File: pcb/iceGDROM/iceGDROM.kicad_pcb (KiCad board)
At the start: 2 copper layers, 60 x 40 mm, 76 parts, among them J1 Conn_02x22_Odd_Even, J2 Micro_SD_Card_Det_Hirose_DM3AT, U1 ICE40HX8K-BG121, U2 ME6206A25M3G_SOT23, U3 LD1117S12TR_SOT223, U4 W25Q32JVSS, X1 SG-310SCF

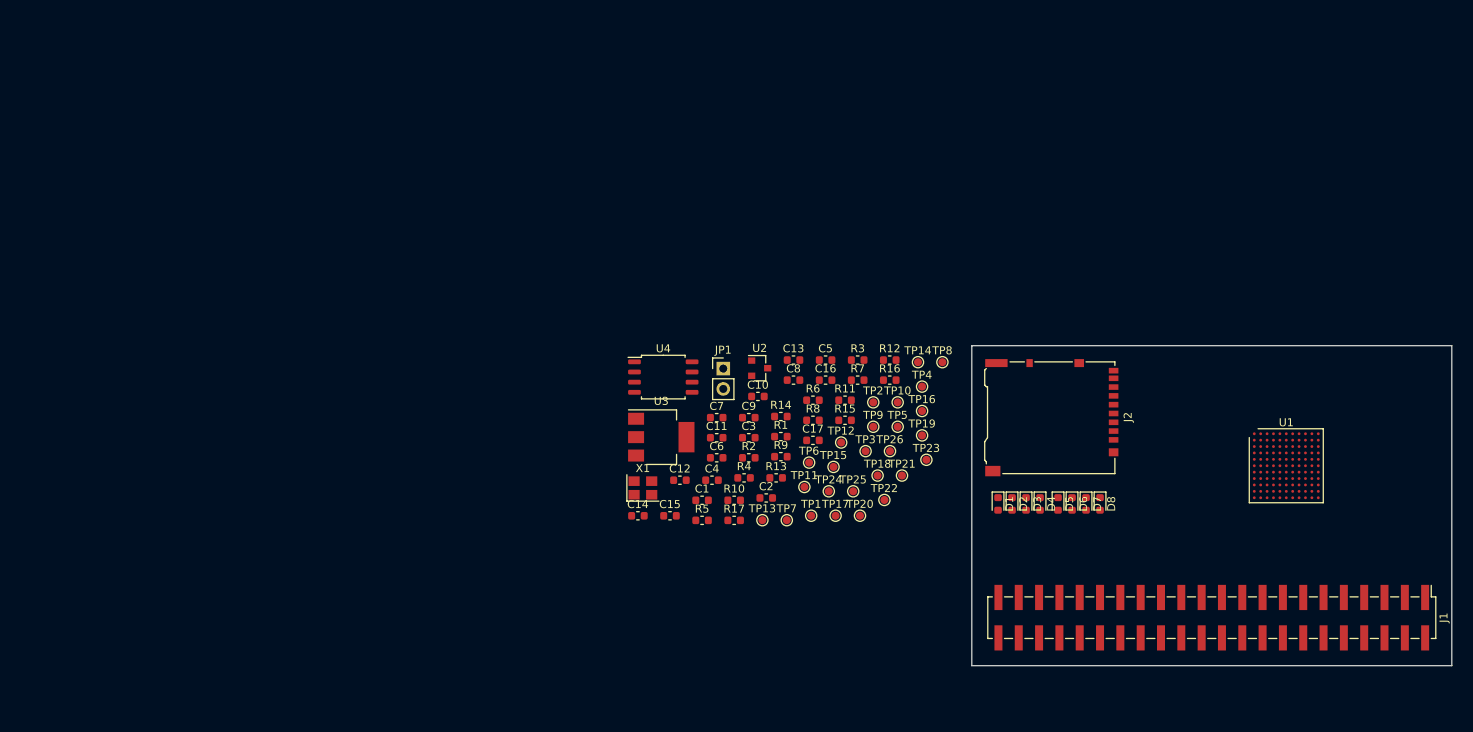
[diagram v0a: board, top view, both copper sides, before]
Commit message: Included the SPI Memory card into the schematic as a major point. Created a footprint for the tactile button being used and including the 3D model due to no NC clause.
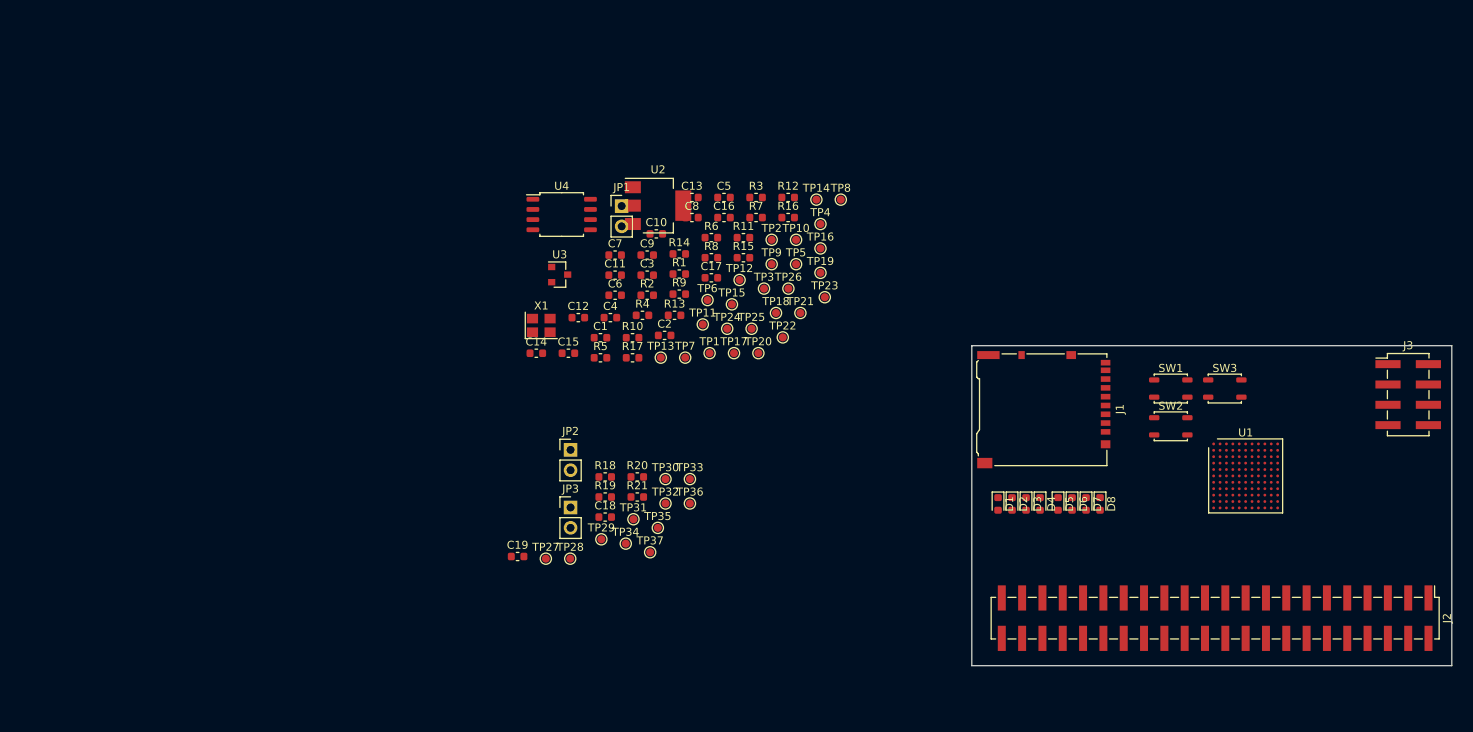
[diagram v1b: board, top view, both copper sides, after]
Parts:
- added C18: 1u0, Capacitor_SMD:C_0603_1608Metric, F.Cu at (109.2, 86.4)
- added C19: 10u, Capacitor_SMD:C_0603_1608Metric, F.Cu at (98.2, 91.4)
- added J3: Conn_02x04_Odd_Even, Connector_PinHeader_2.54mm:PinHeader_2x04_P2.54mm_Vertical_SMD, F.Cu at (209.6, 71.1)
- added JP2: Jumper_NC_Small, Connector_PinHeader_2.54mm:PinHeader_1x02_P2.54mm_Vertical, F.Cu at (104.8, 78.0)
- added JP3: Jumper_NC_Small, Connector_PinHeader_2.54mm:PinHeader_1x02_P2.54mm_Vertical, F.Cu at (104.8, 85.2)
- added R18: 10K, Resistor_SMD:R_0603_1608Metric, F.Cu at (109.2, 81.4)
- added R19: 10K, Resistor_SMD:R_0603_1608Metric, F.Cu at (109.2, 83.9)
- added R20: 100R, Resistor_SMD:R_0603_1608Metric, F.Cu at (113.2, 81.4)
- added R21: 100R, Resistor_SMD:R_0603_1608Metric, F.Cu at (113.2, 83.9)
- added SW1: SW_Push, iceGDROM:SW_Push_SPST_NO_Alps_SKRP, F.Cu at (179.9, 70.4)
- added SW2: SW_Push, iceGDROM:SW_Push_SPST_NO_Alps_SKRP, F.Cu at (179.9, 75.1)
- added SW3: SW_Push, iceGDROM:SW_Push_SPST_NO_Alps_SKRP, F.Cu at (186.6, 70.4)
- added TP27: TestPoint, TestPoint:TestPoint_Pad_D1.0mm, F.Cu at (101.8, 91.6)
- added TP28: TestPoint, TestPoint:TestPoint_Pad_D1.0mm, F.Cu at (104.8, 91.6)
- added TP29: TestPoint, TestPoint:TestPoint_Pad_D1.0mm, F.Cu at (108.7, 89.2)
- added TP30: TestPoint, TestPoint:TestPoint_Pad_D1.0mm, F.Cu at (116.7, 81.7)
- added TP31: TestPoint, TestPoint:TestPoint_Pad_D1.0mm, F.Cu at (112.7, 86.7)
- added TP32: TestPoint, TestPoint:TestPoint_Pad_D1.0mm, F.Cu at (116.7, 84.7)
- added TP33: TestPoint, TestPoint:TestPoint_Pad_D1.0mm, F.Cu at (119.8, 81.7)
- added TP34: TestPoint, TestPoint:TestPoint_Pad_D1.0mm, F.Cu at (111.7, 89.7)
- added TP35: TestPoint, TestPoint:TestPoint_Pad_D1.0mm, F.Cu at (115.8, 87.8)
- added TP36: TestPoint, TestPoint:TestPoint_Pad_D1.0mm, F.Cu at (119.8, 84.7)
- added TP37: TestPoint, TestPoint:TestPoint_Pad_D1.0mm, F.Cu at (114.8, 90.8)
- C11, C12, C17, C2: value 10u -> 100n
- C15, C16, C5: value 100n -> 10u
- C3: value 1u0 -> 10u
- C4: value 100n -> 1u0
- C6: value 10u -> 1u0
- C7: value 1u0 -> 100n
- J1: value Conn_02x22_Odd_Even -> Micro_SD_Card_Det_Hirose_DM3AT; footprint Connector_PinHeader_2.54mm:PinHeader_2x22_P2.54mm_Vertical_SMD -> Connector_Card:microSD_HC_Hirose_DM3AT-SF-PEJM5
- J2: value Micro_SD_Card_Det_Hirose_DM3AT -> Conn_02x22_Odd_Even; footprint Connector_Card:microSD_HC_Hirose_DM3AT-SF-PEJM5 -> Connector_PinHeader_2.54mm:PinHeader_2x22_P2.54mm_Vertical_SMD
- R1, R12, R13, R14, R15, R16, R17, R2, R3, R4, R5, R6, R7, R8: value R -> 10K
- R10, R9: value 100R -> 10K
- U2: value ME6206A25M3G_SOT23 -> LD1117S12TR_SOT223; footprint Package_TO_SOT_SMD:SOT-23 -> Package_TO_SOT_SMD:SOT-223-3_TabPin2
- U3: value LD1117S12TR_SOT223 -> ME6206A25M3G_SOT23; footprint Package_TO_SOT_SMD:SOT-223-3_TabPin2 -> Package_TO_SOT_SMD:SOT-23
- moved J1 33.4 mm to (164.0, 73.0)
- moved J2 32.3 mm to (185.4, 99.1)
- moved R7 24.0 mm to (128.0, 49.0)
- moved TP10 24.0 mm to (133.0, 51.8)
- moved C17 24.0 mm to (122.4, 56.5)
- moved C8 24.0 mm to (120.0, 49.0)
- moved JP1 24.0 mm to (111.2, 47.5)
- moved R10 24.0 mm to (112.6, 64.0)
- moved R13 24.0 mm to (117.8, 61.2)
- moved R17 24.0 mm to (112.6, 66.5)
- moved R3 24.0 mm to (128.0, 46.5)
- moved TP21 24.0 mm to (133.6, 60.9)
- moved TP26 24.0 mm to (132.1, 57.9)
- moved TP5 24.0 mm to (133.0, 54.8)
- moved C10 24.0 mm to (115.6, 51.0)
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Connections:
- net Net-(R4-Pad2) renamed /LED0
- net Net-(R5-Pad2) renamed /LED1
- net Net-(R6-Pad2) renamed /LED2
- net Net-(R7-Pad2) renamed /LED3
- C10 pad 1: Net-(C10-Pad1) -> +1V2
- C10 pad 2: Net-(C10-Pad2) -> GND
- C11 pad 1: Net-(C11-Pad1) -> +1V2
- C11 pad 2: Net-(C11-Pad2) -> GND
- C12 pad 1: Net-(C10-Pad1) -> Net-(C12-Pad1)
- C12 pad 2: Net-(C10-Pad2) -> Net-(C12-Pad2)
- C13 pad 1: +1V2 -> Net-(C13-Pad1)
- C13 pad 2: GND -> Net-(C13-Pad2)
- C15 pad 1: +1V2 -> Net-(C12-Pad1)
- C15 pad 2: GND -> Net-(C12-Pad2)
- C16 pad 1: +1V2 -> Net-(C13-Pad1)
- C16 pad 2: GND -> Net-(C13-Pad2)
- C5 pad 1: +3V3 -> +1V2
- C6 pad 1: +1V2 -> +2V5
- C7 pad 1: +2V5 -> +3V3
- C8 pad 1: +2V5 -> +3V3
- C9 pad 1: Net-(C11-Pad1) -> +2V5
- C9 pad 2: Net-(C11-Pad2) -> GND
- J1 pad 1: /G_RST -> /PB5
- J1 pad 10: /D11 -> /PB7
- J1 pad 11: /D3 -> GND
- J1 pad 2: GND -> /PB6
- J1 pad 3: /D7 -> /PB2
- J1 pad 4: /D8 -> +3V3
- J1 pad 5: /D6 -> /PB1
- J1 pad 6: /D9 -> GND
- J1 pad 7: /D5 -> /PB3
- J1 pad 8: /D10 -> /PB4
- J1 pad 9: /D4 -> GND
- J2 pad 1: Net-(J2-Pad1) -> /G_RST
- J2 pad 10: Net-(J2-Pad10) -> /D11
- J2 pad 11: Net-(J2-Pad11) -> /D3
- J2 pad 2: Net-(J2-Pad2) -> GND
- J2 pad 3: Net-(J2-Pad3) -> /D7
- J2 pad 4: Net-(J2-Pad4) -> /D8
- J2 pad 5: Net-(J2-Pad5) -> /D6
- J2 pad 6: Net-(J2-Pad6) -> /D9
- J2 pad 7: Net-(J2-Pad7) -> /D5
- J2 pad 8: Net-(J2-Pad8) -> /D10
- J2 pad 9: Net-(J2-Pad9) -> /D4
- JP1 pad 2: Net-(JP1-Pad2) -> /FLASH_CSn
- R1 pad 1: Net-(D1-Pad2) -> +3V3
- R1 pad 2: Net-(R1-Pad2) -> /PB7
- R10 pad 1: +1V2 -> Net-(D6-Pad2)
- R10 pad 2: Net-(C10-Pad1) -> /LED5
- R11 pad 1: Net-(R11-Pad1) -> Net-(D7-Pad2)
- R11 pad 2: +3V3 -> /LED6
- R12 pad 1: +3V3 -> Net-(D8-Pad2)
- R12 pad 2: /FPGA_SCK -> /LED7
- R13 pad 1: +3V3 -> Net-(R13-Pad1)
- R13 pad 2: Net-(JP1-Pad2) -> +3V3
- R14 pad 2: Net-(R14-Pad2) -> /FPGA_SCK
- R15 pad 2: Net-(R15-Pad2) -> /FLASH_CSn
- R16 pad 2: Net-(R16-Pad2) -> /FLASH_MOSI|IO0
- R17 pad 2: Net-(R17-Pad2) -> /FLASH_MISO|IO1
- R2 pad 1: Net-(D2-Pad2) -> Net-(R2-Pad1)
- R2 pad 2: Net-(R2-Pad2) -> +3V3
- R3 pad 1: Net-(D3-Pad2) -> GND
- R4 pad 1: Net-(D4-Pad2) -> Net-(D1-Pad2)
- R5 pad 1: Net-(D5-Pad2) -> Net-(D2-Pad2)
- R6 pad 1: Net-(D6-Pad2) -> Net-(D3-Pad2)
- R7 pad 1: Net-(D7-Pad2) -> Net-(D4-Pad2)
- R8 pad 1: Net-(D8-Pad2) -> GND
- R9 pad 1: +1V2 -> Net-(D5-Pad2)
- R9 pad 2: Net-(C11-Pad1) -> /LED4
- TP17 pad 1: Net-(JP1-Pad2) -> /PB0
- TP18 pad 1: /FPGA_SCK -> /PB1
- TP19 pad 1: +1V2 -> /PB2
- TP20 pad 1: +2V5 -> /PB3
- TP21 pad 1: Net-(R14-Pad2) -> /PB4
- TP22 pad 1: Net-(C11-Pad1) -> /PB5
- TP23 pad 1: Net-(C10-Pad1) -> /PB6
- TP24 pad 1: Net-(R15-Pad2) -> /PB7
- TP25 pad 1: Net-(R16-Pad2) -> +12V
- TP26 pad 1: Net-(R17-Pad2) -> +5V
- U1 pad C5: Net-(C10-Pad2) -> Net-(C13-Pad2)
- U1 pad C6: Net-(C10-Pad1) -> Net-(C13-Pad1)
- U1 pad J6: Net-(C11-Pad1) -> Net-(C12-Pad1)
- U1 pad J9: Net-(U1-PadJ9) -> /FPGA_SDI
- U1 pad K9: Net-(U1-PadK9) -> /FPGA_SDO
- U1 pad L6: Net-(C11-Pad2) -> Net-(C12-Pad2)
- U2 pad 2: +2V5 -> +1V2
- U3 pad 2: +1V2 -> +2V5
- U4 pad 1: Net-(JP1-Pad2) -> /FLASH_CSn
- U4 pad 2: Net-(R15-Pad2) -> /FLASH_MISO|IO1
- U4 pad 3: Net-(R16-Pad2) -> /FLASH_~WP~|IO2
- U4 pad 5: Net-(R14-Pad2) -> /FLASH_MOSI|IO0
- U4 pad 7: Net-(R17-Pad2) -> /FLASH_~RST~|IO3
- X1 pad 1: Net-(R11-Pad1) -> Net-(R2-Pad1)

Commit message: Finishing up the peripherals for the FPGA in the schematic, adding the CRESET and CDONE circuits and decoupling for IO power pins.
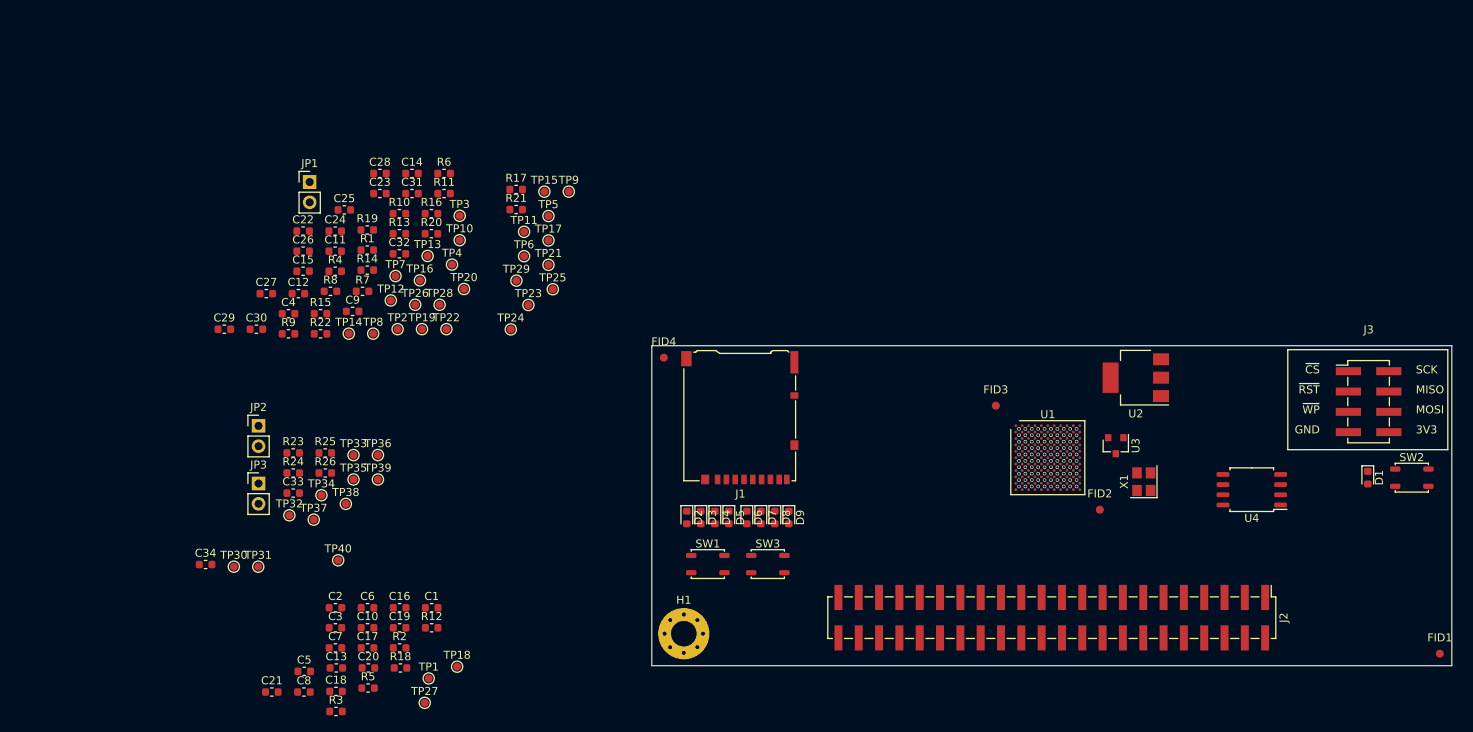
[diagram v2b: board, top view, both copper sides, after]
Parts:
- removed the SW2 at (179.9, 75.1)
- added C1: 10u, Capacitor_SMD:C_0603_1608Metric, F.Cu at (87.5, 97.8)
- added C10: 1u0, Capacitor_SMD:C_0603_1608Metric, F.Cu at (79.5, 100.3)
- added C13: 100n, Capacitor_SMD:C_0603_1608Metric, F.Cu at (75.6, 105.3)
- added C16: 10n, Capacitor_SMD:C_0603_1608Metric, F.Cu at (83.5, 97.8)
- added C17: 10u, Capacitor_SMD:C_0603_1608Metric, F.Cu at (79.5, 102.8)
- added C18: 10n, Capacitor_SMD:C_0603_1608Metric, F.Cu at (75.5, 108.2)
- added C19: 1u0, Capacitor_SMD:C_0603_1608Metric, F.Cu at (83.5, 100.3)
- added C2: 1u0, Capacitor_SMD:C_0603_1608Metric, F.Cu at (75.5, 97.8)
- added C20: 100n, Capacitor_SMD:C_0603_1608Metric, F.Cu at (79.6, 105.3)
- added C21: 10n, Capacitor_SMD:C_0603_1608Metric, F.Cu at (67.5, 108.3)
- added C3: 100n, Capacitor_SMD:C_0603_1608Metric, F.Cu at (75.5, 100.3)
- added C5: 10u, Capacitor_SMD:C_0603_1608Metric, F.Cu at (71.6, 105.7)
- added C6: 1u0, Capacitor_SMD:C_0603_1608Metric, F.Cu at (79.5, 97.8)
- added C7: 100n, Capacitor_SMD:C_0603_1608Metric, F.Cu at (75.5, 102.8)
- added C8: 10u, Capacitor_SMD:C_0603_1608Metric, F.Cu at (71.5, 108.3)
- added D1: LED, LED_SMD:LED_0603_1608Metric, F.Cu at (204.5, 81.5)
- added FID1: Fiducial, Fiducial:Fiducial_1mm_Mask2mm, F.Cu at (213.5, 103.5)
- added FID2: Fiducial, Fiducial:Fiducial_1mm_Mask2mm, F.Cu at (171.0, 85.5)
- added FID3: Fiducial, Fiducial:Fiducial_1mm_Mask2mm, F.Cu at (158.0, 72.5)
- added FID4: Fiducial, Fiducial:Fiducial_1mm_Mask2mm, F.Cu at (116.5, 66.5)
- added H1: MountingHole, MountingHole:MountingHole_3.2mm_M3_Pad_Via, F.Cu at (119.0, 101.0)
- added R12: 10K, Resistor_SMD:R_0603_1608Metric, F.Cu at (87.5, 100.3)
- added R18: 10K, Resistor_SMD:R_0603_1608Metric, F.Cu at (83.6, 105.3)
- added R2: R, Resistor_SMD:R_0603_1608Metric, F.Cu at (83.5, 102.8)
- added R3: 1K, Resistor_SMD:R_0603_1608Metric, F.Cu at (75.5, 110.7)
- added R5: 10K, Resistor_SMD:R_0603_1608Metric, F.Cu at (79.5, 107.8)
- added SW3: SW_Push, iceGDROM:SW_Push_SPST_NO_Alps_SKRP, F.Cu at (129.5, 92.3)
- added TP1: TestPoint, TestPoint:TestPoint_Pad_D1.0mm, F.Cu at (87.1, 106.6)
- added TP18: TestPoint, TestPoint:TestPoint_Pad_D1.0mm, F.Cu at (90.7, 105.1)
- added TP27: TestPoint, TestPoint:TestPoint_Pad_D1.0mm, F.Cu at (86.6, 109.6)
- R21: renamed from R16; value 10K -> NP
- R22: renamed from R17; value 10K -> NP
- moved U4 92.9 mm to (190.0, 83.0), turned to 180 degrees
- moved X1 77.8 mm to (176.5, 82.0), turned to 90 degrees
- moved U3 72.7 mm to (173.0, 77.5), turned to 270 degrees
- moved U2 63.5 mm to (175.5, 69.0), turned to 180 degrees
- moved SW1 61.9 mm to (122.0, 92.3)
- moved TP10 39.1 mm to (91.0, 51.8)
- moved TP3 39.1 mm to (91.0, 48.8)
- moved C11 39.1 mm to (75.4, 53.2)
- moved C12 39.1 mm to (70.8, 58.5)
- moved C14 39.1 mm to (85.0, 43.5)
- moved C15 39.1 mm to (71.4, 55.7)
- moved C22 39.1 mm to (71.4, 50.7)
- moved C23 39.1 mm to (81.0, 46.0)
- moved C24 39.1 mm to (75.4, 50.7)
- moved C25 39.1 mm to (76.6, 48.0)
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- renumbered C3 to C11, C4 to C12, C5 to C14, C6 to C15, C7 to C22, C8 to C23, C9 to C24, C10 to C25, C11 to C26, C12 to C27, C13 to C28, C14 to C29, C15 to C30, C16 to C31, C17 to C32, C18 to C33, C19 to C34, C1 to C4, C2 to C9, D1 to D2, D2 to D3, D3 to D4, D4 to D5, D5 to D6, D6 to D7, D7 to D8, D8 to D9, R6 to R10, R7 to R11, R8 to R13, R9 to R14, R10 to R15, R11 to R16, R12 to R17, R14 to R19, R15 to R20, R18 to R23, R19 to R24, R20 to R25, R21 to R26, R2 to R4, R3 to R6, R13 to R7, R4 to R8, R5 to R9, SW3 to SW2, TP9 to TP10, TP10 to TP11, TP11 to TP12, TP12 to TP13, TP13 to TP14, TP14 to TP15, TP15 to TP16, TP16 to TP17, TP17 to TP19, TP1 to TP2, TP18 to TP20, TP19 to TP21, TP20 to TP22, TP21 to TP23, TP22 to TP24, TP23 to TP25, TP24 to TP26, TP25 to TP28, TP26 to TP29, TP2 to TP3, TP27 to TP30, TP28 to TP31, TP29 to TP32, TP30 to TP33, TP31 to TP34, TP32 to TP35, TP33 to TP36, TP34 to TP37, TP35 to TP38, TP36 to TP39, TP3 to TP4, TP37 to TP40, TP4 to TP5, TP5 to TP6, TP6 to TP7, TP7 to TP8, TP8 to TP9
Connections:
- J3 pad 3: /FLASH_MOSI|IO0 -> /FLASH_~RST~|IO3
- J3 pad 6: /FLASH_~RST~|IO3 -> /FLASH_MOSI|IO0
- J3 pad 8: GND -> +3V3
- JP1 pad 1: /FPGA_CSn -> /FLASH_CSn
- JP1 pad 2: /FLASH_CSn -> Net-(JP1-Pad2)
- R20 pad 2: /FLASH_CSn -> Net-(JP1-Pad2)
- TP33 pad 1: /FLASH_CSn -> Net-(JP1-Pad2)
- U1 pad D6: Net-(U1-PadD6) -> +3V3
- U1 pad E4: Net-(U1-PadE4) -> +3V3
- U1 pad F8: Net-(U1-PadF8) -> +3V3
- U1 pad G4: Net-(U1-PadE4) -> +3V3
- U1 pad H6: Net-(U1-PadH6) -> +3V3
- U1 pad K10: /FPGA_CSn -> /FLASH_CSn
- U4 pad 1: /FLASH_CSn -> Net-(JP1-Pad2)
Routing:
- net (no net): vias 0 -> 100
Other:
- board size 60 x 40 mm -> 100 x 40 mm
- board text added: "3V3"
- board text added: "GND"
- board text added: "MISO"
- board text added: "MOSI"
- board text added: "SCK"
- board text added: "~CS~"
- board text added: "~RST~"
- board text added: "~WP~"
